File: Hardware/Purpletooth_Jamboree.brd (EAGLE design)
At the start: 101.6 x 50.8 mm, 96 parts, among them Q1 MOSFET-NCHANNELBSS138, Q2 MOSFET-NCHANNELBSS138, Q3 MMBT4403, U2 MIC5219 3.3V

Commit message: Roll to next round of protos. - fix FTDI header pinouts - new USB footprint - add resistor to defeat charger temp sense - remove inductor to ground on audio input - fix buttons (add inline resistor, pull to 3.3v instead of ground) - add reset/pair2 button
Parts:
- removed L3: 15nH, SparkFun-Passives:0603
- added JP21, JP22: M02PTH, SparkFun-Connectors:1X02
- added R27, R33: 10K, SparkFun-Resistors:0603-RES
- added R28, R29, R30, R31, R32: 2.2k, SparkFun-Resistors:0603-RES
- added S8: (no value), SparkFun-Electromechanical:TACTILE_SWITCH_SMD
- JP2: value USB-MICROB -> USB_AB""; device SparkFun-Connectors:USB-MICROB -> SparkFun-Connectors:USB-AB-MICRO-SMD_V03
- moved FRAME3 174.9 mm to (12.7, -10.2)
- moved FRAME1 170.2 mm to (12.7, -10.2)
- moved FRAME2 40.7 mm to (12.7, -10.2)
- moved JP4 7.62 mm to (49.5, 8.89)
- moved JP5 7.62 mm to (41.9, 8.89)
- moved S2 7.62 mm to (50.8, 5.08)
- moved S3 7.62 mm to (43.2, 5.08)
- moved C16 2.99 mm to (18.5, 40.5), turned to 180 degrees
- moved JP2 0.51 mm to (99.6, 35.6), turned to 180 degrees
- renumbered U$1 to U3
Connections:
- removed net IN_GND: JP14.SLEEVE, JP18.3, L3.2
- new net N$1: JP21.2, R27.2, U3.5
- new net N$10: JP4.2, R28.1, S2.2
- new net N$11: JP5.2, R29.1, S3.2
- new net N$14: JP7.2, R30.1, S4.2
- new net N$15: JP8.2, R31.1, S5.2
- new net N$22: JP9.2, R32.1, S6.2
- net !RESET: now also JP22.2, S8.2
- net 3.3V: now also JP3.1, JP4.1, JP5.1, JP7.1, JP8.1, JP9.1, R27.1, S1.4, S2.4, S3.4, S4.4, S5.4, S6.4
- net 5V_RX: now also JP19.P$3; no longer JP19.P$2
- net 5V_TX: now also JP19.P$2; no longer JP19.P$3
- net AIO_1: now also R33.1
- net GND: now also JP14.SLEEVE, JP18.3, JP2.GND1, JP21.1, JP22.1, S8.4; no longer JP2.GND, JP2.MT1, JP2.MT2, JP3.1, JP4.1, JP5.1, JP7.1, JP8.1, JP9.1, L3.1, S1.4, S2.4, S3.4, S4.4, S5.4, S6.4
- net PIO_0: now also R28.2; no longer JP4.2, S2.2
- net PIO_1: now also R29.2; no longer JP5.2, S3.2
- net PIO_2: now also R30.2; no longer JP7.2, S4.2
- net PIO_4: now also R31.2; no longer JP8.2, S5.2
- net PIO_5: now also R32.2; no longer JP9.2, S6.2
- net USB_N: now also JP2.D-1; no longer JP2.D-
- net USB_P: now also JP2.D+1; no longer JP2.D+
- net VIN: now also R33.2
- net V_USB: now also JP2.VBUS1; no longer JP2.VBUS
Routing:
- net 3.3V: track 249.2 -> 372.9 mm, vias 8 -> 9
- net !RESET: track 12.6 -> 61.5 mm, vias 2 -> 4
- net VIN: track 102.8 -> 133.6 mm, vias 5 -> 7
- net N$1: track 0.00 -> 16.8 mm, vias 0 -> 2
- net IN_GND: track 9.85 -> 0.00 mm
- net PIO_2: track 68.0 -> 58.8 mm, vias 1 -> 2
- net AIO_1: track 18.7 -> 26.2 mm, vias 1 -> 2
- net PIO_0: track 32.8 -> 25.6 mm
- net N$11: track 0.00 -> 5.81 mm
- net N$14: track 0.00 -> 5.74 mm
- net N$10: track 0.00 -> 5.74 mm
- net N$22: track 0.00 -> 5.74 mm
- net N$15: track 0.00 -> 5.74 mm
- net PIO_4: track 35.8 -> 33.1 mm, vias 1 -> 2
- net PIO_5: track 51.8 -> 49.4 mm
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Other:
- board text added: "M. Hord"
- board text added: "PAIR 2"
- board text added: "PIO_0"
- board text added: "PIO_1"
- board text added: "PIO_2"
- board text added: "PIO_4"
- board text added: "PIO_5"
- board text added: "RESET"
- board text added: "VREGEN"
- board text added: "v02"
- board text removed: "IN_GND"
- board text removed: "v01"

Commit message: Library update for connectors lib
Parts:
- JP2: value USB_AB"" -> (none)
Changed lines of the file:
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@@
 <layers>
 <layer number="1" name="Top" color="4" fill="1" visible="yes" active="yes"/>
-<layer number="2" name="Route2" color="1" fill="3" visible="yes" active="yes"/>
-<layer number="15" name="Route15" color="4" fill="6" visible="yes" active="yes"/>
+<layer number="2" name="Route2" color="1" fill="3" visible="no" active="yes"/>
+<layer number="15" name="Route15" color="4" fill="6" visible="no" active="yes"/>
 <layer number="16" name="Bottom" color="1" fill="1" visible="yes" active="yes"/>
 <layer number="17" name="Pads" color="2" fill="1" visible="yes" active="yes"/>
@@
 <layer number="23" name="tOrigins" color="15" fill="1" visible="yes" active="yes"/>
 <layer number="24" name="bOrigins" color="15" fill="1" visible="yes" active="yes"/>
-<layer number="25" name="tNames" color="7" fill="1" visible="yes" active="yes"/>
-<layer number="26" name="bNames" color="7" fill="1" visible="yes" active="yes"/>
-<layer number="27" name="tValues" color="7" fill="1" visible="yes" active="yes"/>
-<layer number="28" name="bValues" color="7" fill="1" visible="yes" active="yes"/>
-<layer number="29" name="tStop" color="7" fill="3" visible="yes" active="yes"/>
-<layer number="30" name="bStop" color="7" fill="6" visible="yes" active="yes"/>
-<layer number="31" name="tCream" color="7" fill="4" visible="yes" active="yes"/>
-<layer number="32" name="bCream" color="7" fill="5" visible="yes" active="yes"/>
-<layer number="39" name="tKeepout" color="4" fill="11" visible="yes" active="yes"/>
-<layer number="40" name="bKeepout" color="1" fill="11" visible="yes" active="yes"/>
-<layer number="41" name="tRestrict" color="4" fill="10" visible="yes" active="yes"/>
-<layer number="42" name="bRestrict" color="1" fill="10" visible="yes" active="yes"/>
-<layer number="43" name="vRestrict" color="2" fill="10" visible="yes" active="yes"/>
-<layer number="44" name="Drills" color="7" fill="1" visible="yes" active="yes"/>
+<layer number="25" name="tNames" color="7" fill="1" visible="no" active="yes"/>
+<layer number="26" name="bNames" color="7" fill="1" visible="no" active="yes"/>
+<layer number="27" name="tValues" color="7" fill="1" visible="no" active="yes"/>
+<layer number="28" name="bValues" color="7" fill="1" visible="no" active="yes"/>
+<layer number="29" name="tStop" color="7" fill="3" visible="no" active="yes"/>
+<layer number="30" name="bStop" color="7" fill="6" visible="no" active="yes"/>
+<layer number="31" name="tCream" color="7" fill="4" visible="no" active="yes"/>
+<layer number="32" name="bCream" color="7" fill="5" visible="no" active="yes"/>
+<layer number="39" name="tKeepout" color="4" fill="11" visible="no" active="yes"/>
+<layer number="40" name="bKeepout" color="1" fill="11" visible="no" active="yes"/>
+<layer number="41" name="tRestrict" color="4" fill="10" visible="no" active="yes"/>
+<layer number="42" name="bRestrict" color="1" fill="10" visible="no" active="yes"/>
+<layer number="43" name="vRestrict" color="2" fill="10" visible="no" active="yes"/>
+<layer number="44" name="Drills" color="7" fill="1" visible="no" active="yes"/>
 <layer number="45" name="Holes" color="7" fill="1" visible="yes" active="yes"/>
-<layer number="46" name="Milling" color="3" fill="1" visible="yes" active="yes"/>
+<layer number="46" name="Milling" color="3" fill="1" visible="no" active="yes"/>
 <layer number="51" name="tDocu" color="6" fill="1" visible="yes" active="yes"/>
-<layer number="52" name="bDocu" color="7" fill="1" visible="yes" active="yes"/>
+<layer number="52" name="bDocu" color="7" fill="1" visible="no" active="yes"/>
 <layer number="3" name="Route3" color="4" fill="3" visible="no" active="no"/>
 <layer number="4" name="Route4" color="1" fill="4" visible="no" active="no"/>
@@
 </element>
 <element name="FRAME2" library="SparkFun-Aesthetics" package="CREATIVE_COMMONS" value="FRAME-LETTER" x="12.7" y="-10.16"/>
-<element name="JP2" library="SparkFun-Connectors" package="USB-AB-MICRO-SMD_V03" value="USB_AB&quot;&quot;" x="99.568" y="35.56" rot="R180"/>
+<element name="JP2" library="SparkFun-Connectors" package="USB-AB-MICRO-SMD_V03" value="" x="99.568" y="35.56" rot="R180">
+<attribute name="PROD_ID" value="CONN-11794" x="99.568" y="35.56" size="1.778" layer="27" rot="R180" display="off"/>
+</element>
 <element name="JP3" library="SparkFun-Connectors" package="1X02" value="M02PTH" x="31.75" y="8.89"/>
 <element name="FRAME3" library="SparkFun-Aesthetics" package="CREATIVE_COMMONS" value="FRAME-LETTER" x="12.7" y="-10.16"/>
@@
 </signal>
 </signals>
-<errors>
-</errors>
 </board>
 </drawing>

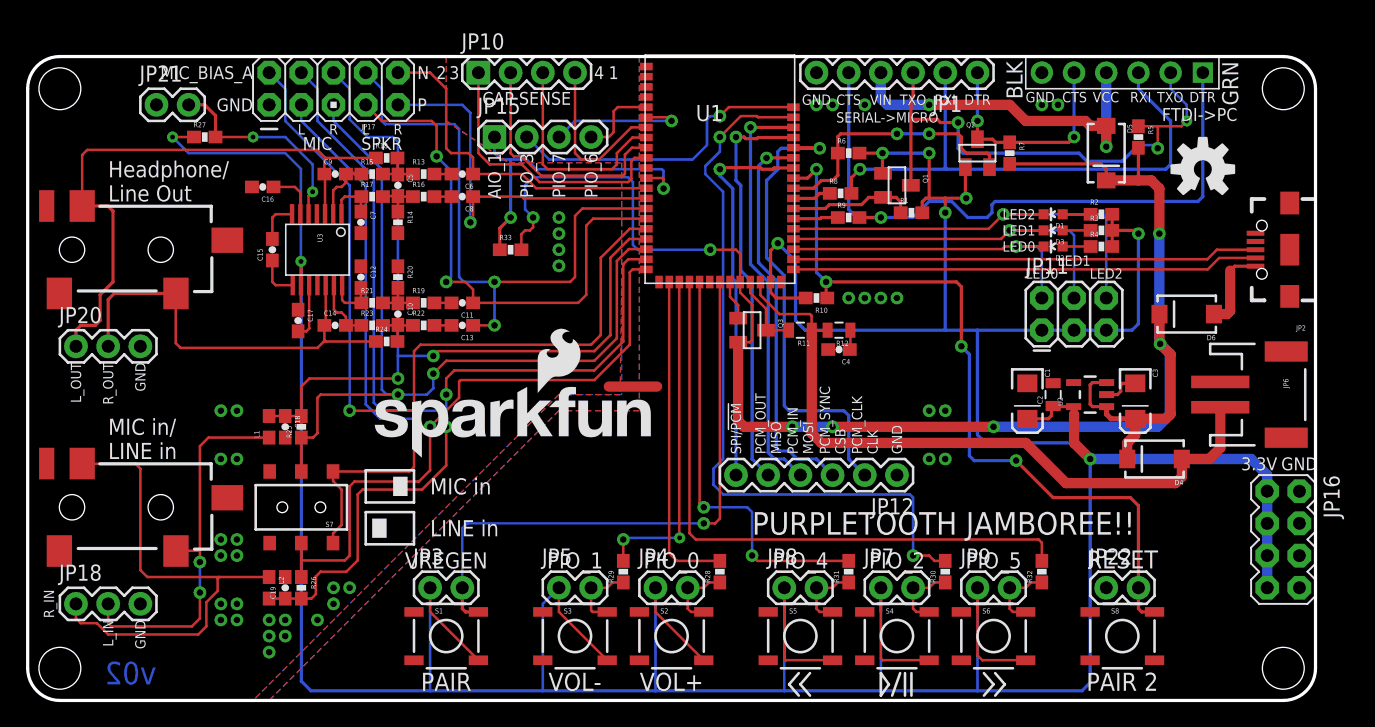
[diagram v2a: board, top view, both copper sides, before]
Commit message: Transition to v10 for production - change labels on board and schematic - move top edge of board .05" up, to prevent module overhang from   interfering with panelization
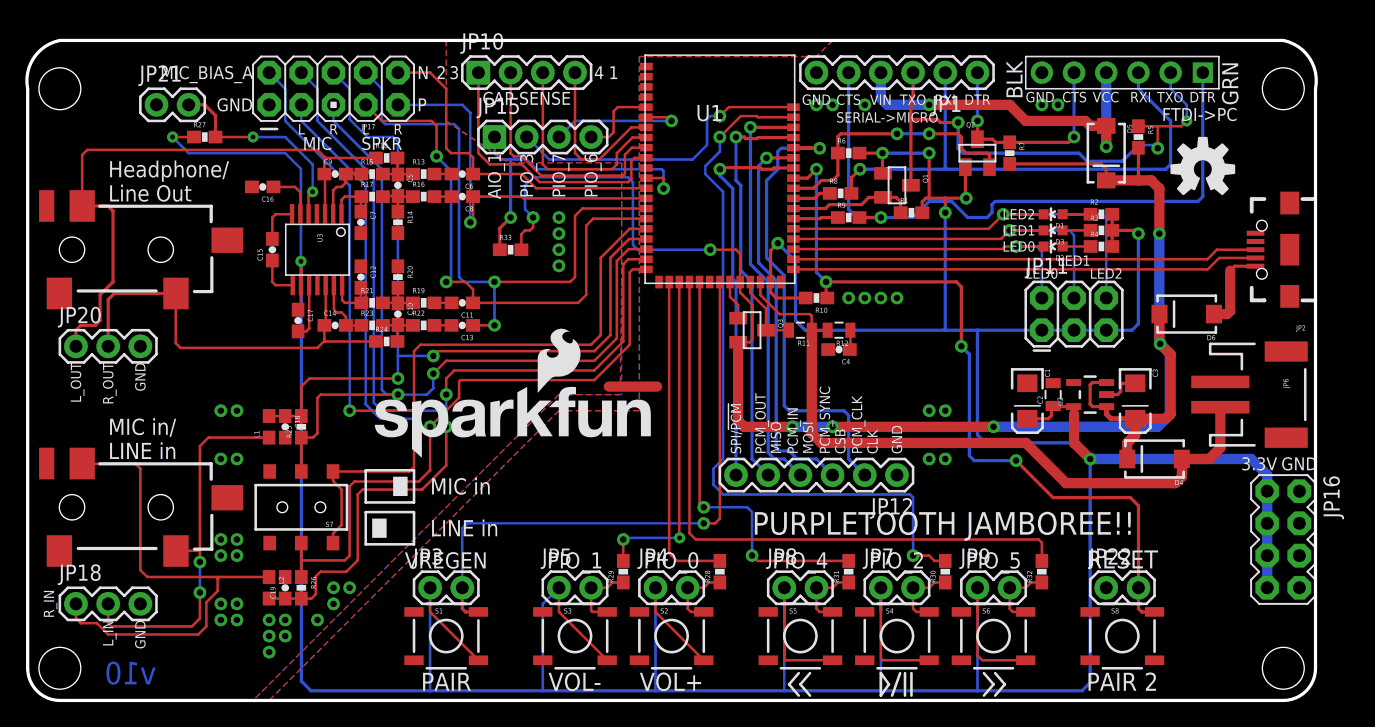
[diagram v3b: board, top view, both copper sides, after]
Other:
- board size 101.6 x 50.8 mm -> 101.7 x 52.1 mm
- board text added: "v10"
- board text removed: "v02"
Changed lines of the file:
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@@
 <wire x1="99.06" y1="0" x2="101.6" y2="2.54" width="0.254" layer="20" curve="90"/>
 <wire x1="101.6" y1="2.54" x2="101.6" y2="48.26" width="0.254" layer="20"/>
-<wire x1="101.6" y1="48.26" x2="99.06" y2="50.8" width="0.254" layer="20" curve="90"/>
-<wire x1="99.06" y1="50.8" x2="2.54" y2="50.8" width="0.254" layer="20"/>
-<wire x1="2.54" y1="50.8" x2="0" y2="48.26" width="0.254" layer="20" curve="90"/>
+<wire x1="101.6" y1="48.26" x2="99.06" y2="52.07" width="0.254" layer="20" curve="90"/>
+<wire x1="99.06" y1="52.07" x2="2.54" y2="52.07" width="0.254" layer="20"/>
+<wire x1="2.54" y1="52.07" x2="0" y2="48.26" width="0.254" layer="20" curve="90"/>
 <text x="33.02" y="0.762" size="1.4224" layer="21" font="vector" ratio="15" align="bottom-center">PAIR</text>
 <text x="43.18" y="0.762" size="1.4224" layer="21" font="vector" ratio="15" align="bottom-center">VOL-</text>
@@
 <text x="44.45" y="43.18" size="1.016" layer="21" font="vector" ratio="15" rot="R270" align="center-left">PIO_6</text>
 <text x="57.15" y="13.97" size="1.778" layer="21" font="vector" ratio="15" align="center-left">PURPLETOOTH JAMBOREE!!</text>
-<text x="10.16" y="1.27" size="1.778" layer="16" font="vector" ratio="15" rot="MR0">v02</text>
+<text x="10.16" y="1.27" size="1.778" layer="16" font="vector" ratio="15" rot="MR0">v10</text>
 <text x="3.81" y="26.67" size="0.8128" layer="21" font="vector" ratio="15" rot="R270" align="center-left">L_OUT</text>
 <text x="6.35" y="26.67" size="0.8128" layer="21" font="vector" ratio="15" rot="R270" align="center-left">R_OUT</text>
@@
 <contactref element="JP17" pad="1"/>
 <polygon width="0.2032" layer="16" isolate="0.3048">
-<vertex x="33.02" y="50.8"/>
+<vertex x="33.02" y="52.07"/>
 <vertex x="33.02" y="45.72"/>
 <vertex x="37.973" y="42.418"/>
@@
 <vertex x="0" y="2.54"/>
 <vertex x="0" y="48.26" curve="-90"/>
-<vertex x="2.54" y="50.8"/>
+<vertex x="2.54" y="52.07"/>
 </polygon>
 <polygon width="0.2032" layer="1" isolate="0.3048">
-<vertex x="33.02" y="50.8"/>
+<vertex x="33.02" y="52.07"/>
 <vertex x="33.02" y="45.72"/>
 <vertex x="37.973" y="42.418"/>
@@
 <vertex x="0" y="2.54"/>
 <vertex x="0" y="48.26" curve="-90"/>
-<vertex x="2.54" y="50.8"/>
+<vertex x="2.54" y="52.07"/>
 </polygon>
 <via x="41.91" y="38.1" extent="1-16" drill="0.508"/>
@@
 <vertex x="101.6" y="2.54"/>
 <vertex x="101.6" y="48.26" curve="90"/>
-<vertex x="99.06" y="50.8"/>
+<vertex x="99.06" y="52.07"/>
+<vertex x="63.5" y="52.07"/>
+<vertex x="62.23" y="50.8"/>
 </polygon>
 <polygon width="0.254" layer="1" isolate="0.3048">
@@
 <vertex x="101.6" y="2.54"/>
 <vertex x="101.6" y="48.26" curve="90"/>
-<vertex x="99.06" y="50.8"/>
+<vertex x="99.06" y="52.07"/>
+<vertex x="63.5" y="52.07"/>
+<vertex x="62.23" y="50.8"/>
 </polygon>
 <wire x1="45.847" y1="24.765" x2="49.657" y2="24.765" width="0.8128" layer="1"/>

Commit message: Added micro fiducial to board
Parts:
- removed FRAME2, FRAME3: FRAME-LETTER, SparkFun-Aesthetics:CREATIVE_COMMONS
- added FID1, FID2: FIDUCIALUFIDUCIAL, SparkFun-Aesthetics:MICRO-FIDUCIAL
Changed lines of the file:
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@@
 <?xml version="1.0" encoding="utf-8"?>
 <!DOCTYPE eagle SYSTEM "eagle.dtd">
-<eagle version="6.4">
+<eagle version="6.5.0">
 <drawing>
 <settings>
@@
 <setting verticaltext="up"/>
 </settings>
-<grid distance="0.05" unitdist="inch" unit="inch" style="lines" multiple="1" display="yes" altdistance="0.005" altunitdist="inch" altunit="inch"/>
+<grid distance="0.05" unitdist="inch" unit="inch" style="lines" multiple="1" display="yes" altdistance="0.01" altunitdist="inch" altunit="inch"/>
 <layers>
 <layer number="1" name="Top" color="4" fill="1" visible="yes" active="yes"/>
-<layer number="2" name="Route2" color="1" fill="3" visible="no" active="yes"/>
-<layer number="15" name="Route15" color="4" fill="6" visible="no" active="yes"/>
+<layer number="2" name="Route2" color="1" fill="3" visible="yes" active="yes"/>
+<layer number="15" name="Route15" color="4" fill="6" visible="yes" active="yes"/>
 <layer number="16" name="Bottom" color="1" fill="1" visible="yes" active="yes"/>
 <layer number="17" name="Pads" color="2" fill="1" visible="yes" active="yes"/>
 <layer number="18" name="Vias" color="2" fill="1" visible="yes" active="yes"/>
 <layer number="19" name="Unrouted" color="6" fill="1" visible="yes" active="yes"/>
-<layer number="20" name="Dimension" color="15" fill="1" visible="yes" active="yes"/>
-<layer number="21" name="tPlace" color="16" fill="1" visible="yes" active="yes"/>
-<layer number="22" name="bPlace" color="14" fill="1" visible="yes" active="yes"/>
+<layer number="20" name="Dimension" color="6" fill="1" visible="yes" active="yes"/>
+<layer number="21" name="tPlace" color="6" fill="1" visible="yes" active="yes"/>
+<layer number="22" name="bPlace" color="6" fill="1" visible="yes" active="yes"/>
 <layer number="23" name="tOrigins" color="15" fill="1" visible="yes" active="yes"/>
 <layer number="24" name="bOrigins" color="15" fill="1" visible="yes" active="yes"/>
-<layer number="25" name="tNames" color="7" fill="1" visible="no" active="yes"/>
-<layer number="26" name="bNames" color="7" fill="1" visible="no" active="yes"/>
-<layer number="27" name="tValues" color="7" fill="1" visible="no" active="yes"/>
-<layer number="28" name="bValues" color="7" fill="1" visible="no" active="yes"/>
-<layer number="29" name="tStop" color="7" fill="3" visible="no" active="yes"/>
-<layer number="30" name="bStop" color="7" fill="6" visible="no" active="yes"/>
-<layer number="31" name="tCream" color="7" fill="4" visible="no" active="yes"/>
-<layer number="32" name="bCream" color="7" fill="5" visible="no" active="yes"/>
-<layer number="39" name="tKeepout" color="4" fill="11" visible="no" active="yes"/>
-<layer number="40" name="bKeepout" color="1" fill="11" visible="no" active="yes"/>
-<layer number="41" name="tRestrict" color="4" fill="10" visible="no" active="yes"/>
-<layer number="42" name="bRestrict" color="1" fill="10" visible="no" active="yes"/>
-<layer number="43" name="vRestrict" color="2" fill="10" visible="no" active="yes"/>
-<layer number="44" name="Drills" color="7" fill="1" visible="no" active="yes"/>
+<layer number="25" name="tNames" color="7" fill="1" visible="yes" active="yes"/>
+<layer number="26" name="bNames" color="7" fill="1" visible="yes" active="yes"/>
+<layer number="27" name="tValues" color="7" fill="1" visible="yes" active="yes"/>
+<layer number="28" name="bValues" color="7" fill="1" visible="yes" active="yes"/>
+<layer number="29" name="tStop" color="7" fill="3" visible="yes" active="yes"/>
+<layer number="30" name="bStop" color="7" fill="6" visible="yes" active="yes"/>
+<layer number="31" name="tCream" color="7" fill="4" visible="yes" active="yes"/>
+<layer number="32" name="bCream" color="7" fill="5" visible="yes" active="yes"/>
+<layer number="39" name="tKeepout" color="4" fill="11" visible="yes" active="yes"/>
+<layer number="40" name="bKeepout" color="1" fill="11" visible="yes" active="yes"/>
+<layer number="41" name="tRestrict" color="4" fill="10" visible="yes" active="yes"/>
+<layer number="42" name="bRestrict" color="1" fill="10" visible="yes" active="yes"/>
+<layer number="43" name="vRestrict" color="2" fill="10" visible="yes" active="yes"/>
+<layer number="44" name="Drills" color="7" fill="1" visible="yes" active="yes"/>
 <layer number="45" name="Holes" color="7" fill="1" visible="yes" active="yes"/>
-<layer number="46" name="Milling" color="3" fill="1" visible="no" active="yes"/>
+<layer number="46" name="Milling" color="3" fill="1" visible="yes" active="yes"/>
 <layer number="51" name="tDocu" color="6" fill="1" visible="yes" active="yes"/>
-<layer number="52" name="bDocu" color="7" fill="1" visible="no" active="yes"/>
+<layer number="52" name="bDocu" color="7" fill="1" visible="yes" active="yes"/>
 <layer number="3" name="Route3" color="4" fill="3" visible="no" active="no"/>
 <layer number="4" name="Route4" color="1" fill="4" visible="no" active="no"/>
@@
 <attribute name="PROD_ID" value="RES-08272" x="21.59" y="8.89" size="1.778" layer="27" font="vector" ratio="15" rot="R270" display="off"/>
 </element>
-<element name="FRAME2" library="SparkFun-Aesthetics" package="CREATIVE_COMMONS" value="FRAME-LETTER" x="12.7" y="-10.16"/>
 <element name="JP2" library="SparkFun-Connectors" package="USB-AB-MICRO-SMD_V03" value="" x="99.568" y="35.56" rot="R180">
 <attribute name="PROD_ID" value="CONN-11794" x="99.568" y="35.56" size="1.778" layer="27" rot="R180" display="off"/>
 </element>
 <element name="JP3" library="SparkFun-Connectors" package="1X02" value="M02PTH" x="31.75" y="8.89"/>
-<element name="FRAME3" library="SparkFun-Aesthetics" package="CREATIVE_COMMONS" value="FRAME-LETTER" x="12.7" y="-10.16"/>
 <element name="JP4" library="SparkFun-Connectors" package="1X02" value="M02PTH" x="49.53" y="8.89"/>
 <element name="JP5" library="SparkFun-Connectors" package="1X02" value="M02PTH" x="41.91" y="8.89"/>
@@
 <attribute name="PROD_ID" value="RES-00824" x="38.1" y="35.56" size="1.778" layer="27" font="vector" ratio="15" display="off"/>
 </element>
+<element name="FID1" library="SparkFun-Aesthetics" package="MICRO-FIDUCIAL" value="FIDUCIALUFIDUCIAL" x="6.35" y="49.53"/>
+<element name="FID2" library="SparkFun-Aesthetics" package="MICRO-FIDUCIAL" value="FIDUCIALUFIDUCIAL" x="93.98" y="5.08"/>
 </elements>
 <signals>
@@
 <vertex x="41.91" y="24.13"/>
 <vertex x="38.1" y="20.32"/>
-<vertex x="38.1" y="20.32"/>
 <vertex x="17.78" y="0"/>
